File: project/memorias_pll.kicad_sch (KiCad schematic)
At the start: 34 parts, among them U5 M93C66, U6 ICE40HX4K-TQ144, U7 W25X40CLSN

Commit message: - Included properties such as Reference, Value, Footprint, and various manufacturer details. - Defined 20 pins with appropriate names and attributes for the symbol. - Ensured compatibility with KiCad version 8.0 and above.
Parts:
- D3: footprint Diode_SMD:D_1206_3216Metric -> (none)

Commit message: Agregados footprints de todos los componentes
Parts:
- D3: footprint (none) -> Diode_SMD:D_1206_3216Metric_Pad1.42x1.75mm_HandSolder
- D4: value LED -> LED Red; footprint libraries:WL-SMTW_3528 -> 150141RS73100(LED):LEDM3528X210N
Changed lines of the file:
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@@
 			)
 		)
-		(property "Value" "LED"
+		(property "Value" "LED Red"
 			(at 141.986 153.162 0)
 			(effects
@@
 			)
 		)
-		(property "Footprint" "libraries:WL-SMTW_3528"
+		(property "Footprint" "150141RS73100(LED):LEDM3528X210N"
 			(at 143.51 148.59 0)
 			(effects
@@
 			)
 		)
-		(property "Footprint" ""
+		(property "Footprint" "Diode_SMD:D_1206_3216Metric_Pad1.42x1.75mm_HandSolder"
 			(at 128.27 142.24 0)
 			(effects

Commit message: Ruteo critico finalizado
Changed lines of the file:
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@@
 (kicad_sch
-	(version 20231120)
+	(version 20250114)
 	(generator "eeschema")
-	(generator_version "8.0")
+	(generator_version "9.0")
 	(paper "A4")
+	(rectangle
+		(start 203.2 99.06)
+		(end 228.6 123.19)
+		(stroke
+			(width 0.25)
+			(type dash)
+		)
+		(fill
+			(type none)
+		)
+	)
+	(rectangle
+		(start 195.58 129.54)
+		(end 229.87 154.94)
+		(stroke
+			(width 0.25)
+			(type dash)
+		)
+		(fill
+			(type none)
+		)
+	)
+	(rectangle
+		(start 157.48 35.56)
+		(end 168.91 60.96)
+		(stroke
+			(width 0.25)
+			(type dash)
+		)
+		(fill
+			(type none)
+		)
+	)
+	(rectangle
+		(start 184.15 34.29)
+		(end 233.68 64.77)
+		(stroke
+			(width 0.25)
+			(type dash)
+		)
+		(fill
+			(type none)
+		)
+	)
+	(rectangle
+		(start 85.09 74.93)
+		(end 233.68 157.48)
+		(stroke
+			(width 0.25)
+			(type dash)
+		)
+		(fill
+			(type none)
+		)
+	)
+	(rectangle
+		(start 85.09 31.75)
+		(end 172.72 66.04)
+		(stroke
+			(width 0.25)
+			(type dash)
+		)
+		(fill
+			(type none)
+		)
+	)
+	(rectangle
+		(start 151.13 92.71)
+		(end 171.45 100.33)
+		(stroke
+			(width 0.25)
+			(type dash)
+		)
+		(fill
+			(type none)
+		)
+	)
+	(text "Desacople FPGA VCC\n"
+		(exclude_from_sim no)
+		(at 207.01 132.08 0)
+		(effects
+			(font
+				(size 1.27 1.27)
+			)
+		)
+	)
+	(text "R12 a R16 son de 220 Ohms"
+		(exclude_from_sim no)
+		(at 149.606 103.886 0)
+		(effects
+			(font
+				(size 1.27 1.27)
+			)
+			(justify left)
+		)
+	)
+	(text "Filtro PLL"
+		(exclude_from_sim no)
+		(at 189.738 36.83 0)
+		(effects
+			(font
+				(size 1.27 1.27)
+			)
+		)
+	)
+	(text "EEPROM"
+		(exclude_from_sim no)
+		(at 89.916 34.544 0)
+		(effects
+			(font
+				(size 1.27 1.27)
+			)
+		)
+	)
+	(text "R20 es un resistor de pull-up\nbasado en el esquemático de IceStick.\nRemover en caso de ser innecesario"
+		(exclude_from_sim no)
+		(at 179.832 87.63 0)
+		(effects
+			(font
+				(size 1.27 1.27)
+			)
+			(justify left)
+		)
+	)
+	(text "Desacople W25X40CLSN\n"
+		(exclude_from_sim no)
+		(at 215.646 101.854 0)
+		(effects
+			(font
+				(size 1.27 1.27)
+			)
+		)
+	)
+	(text "Memoria Flash y PLL"
+		(exclude_from_sim no)
+		(at 96.52 77.724 0)
+		(effects
+			(font
+				(size 1.27 1.27)
+			)
+		)
+	)
+	(text "Desacople M93C66"
+		(exclude_from_sim no)
+		(at 162.052 34.29 0)
+		(effects
+			(font
+				(size 1.27 1.27)
+			)
+		)
+	)
 	(junction
 		(at 217.17 52.07)
@@
 		)
 	)
-	(rectangle
-		(start 203.2 99.06)
-		(end 228.6 123.19)
-		(stroke
-			(width 0.25)
-			(type dash)
-		)
-		(fill
-			(type none)
-		)
-	)
-	(rectangle
-		(start 195.58 129.54)
-		(end 229.87 154.94)
-		(stroke
-			(width 0.25)
-			(type dash)
-		)
-		(fill
-			(type none)
-		)
-	)
-	(rectangle
-		(start 157.48 35.56)
-		(end 168.91 60.96)
-		(stroke
-			(width 0.25)
-			(type dash)
-		)
-		(fill
-			(type none)
-		)
-	)
-	(rectangle
-		(start 184.15 34.29)
-		(end 233.68 64.77)
-		(stroke
-			(width 0.25)
-			(type dash)
-		)
-		(fill
-			(type none)
-		)
-	)
-	(rectangle
-		(start 85.09 74.93)
-		(end 233.68 157.48)
-		(stroke
-			(width 0.25)
-			(type dash)
-		)
-		(fill
-			(type none)
-		)
-	)
-	(rectangle
-		(start 85.09 31.75)
-		(end 172.72 66.04)
-		(stroke
-			(width 0.25)
-			(type dash)
-		)
-		(fill
-			(type none)
-		)
-	)
-	(rectangle
-		(start 151.13 92.71)
-		(end 171.45 100.33)
-		(stroke
-			(width 0.25)
-			(type dash)
-		)
-		(fill
-			(type none)
-		)
-	)
-	(text "Desacople FPGA VCC\n"
-		(exclude_from_sim no)
-		(at 207.01 132.08 0)
-		(effects
-			(font
-				(size 1.27 1.27)
-			)
-		)
-	)
-	(text "R12 a R16 son de 220 Ohms"
-		(exclude_from_sim no)
-		(at 149.606 103.886 0)
-		(effects
-			(font
-				(size 1.27 1.27)
-			)
-			(justify left)
-		)
-	)
-	(text "Filtro PLL"
-		(exclude_from_sim no)
-		(at 189.738 36.83 0)
-		(effects
-			(font
-				(size 1.27 1.27)
-			)
-		)
-	)
-	(text "EEPROM"
-		(exclude_from_sim no)
-		(at 89.916 34.544 0)
-		(effects
-			(font
-				(size 1.27 1.27)
-			)
-		)
-	)
-	(text "R20 es un resistor de pull-up\nbasado en el esquemático de IceStick.\nRemover en caso de ser innecesario"
-		(exclude_from_sim no)
-		(at 179.832 87.63 0)
-		(effects
-			(font
-				(size 1.27 1.27)
-			)
-			(justify left)
-		)
-	)
-	(text "Desacople W25X40CLSN\n"
-		(exclude_from_sim no)
-		(at 215.646 101.854 0)
-		(effects
-			(font
-				(size 1.27 1.27)
-			)
-		)
-	)
-	(text "Memoria Flash y PLL"
-		(exclude_from_sim no)
-		(at 96.52 77.724 0)
-		(effects
-			(font
-				(size 1.27 1.27)
-			)
-		)
-	)
-	(text "Desacople M93C66"
-		(exclude_from_sim no)
-		(at 162.052 34.29 0)
-		(effects
-			(font
-				(size 1.27 1.27)
-			)
-		)
-	)
 	(label "VCCPLL1"
 		(at 222.25 48.26 0)
-		(fields_autoplaced yes)
 		(effects
 			(font
@@
 	(label "VCCPLL2"
 		(at 222.25 52.07 0)
-		(fields_autoplaced yes)
 		(effects
 			(font
@@
 	(label "GNDPLL2"
 		(at 223.52 62.23 0)
-		(fields_autoplaced yes)
 		(effects
 			(font
@@
 	(label "GNDPLL2"
 		(at 123.19 91.44 90)
-		(fields_autoplaced yes)
 		(effects
 			(font
@@
 	(label "VCCPLL2"
 		(at 123.19 133.35 270)
-		(fields_autoplaced yes)
 		(effects
 			(font
@@
 	(label "GNDPLL1"
 		(at 120.65 91.44 90)
-		(fields_autoplaced yes)
 		(effects
 			(font
@@
 	(label "GNDPLL1"
 		(at 222.25 38.1 0)
-		(fields_autoplaced yes)
 		(effects
 			(font
@@
 	(label "VCCPLL1"
 		(at 120.65 133.35 270)
-		(fields_autoplaced yes)
 		(effects
 			(font
@@
 		(shape input)
 		(at 153.67 90.17 90)
-		(fields_autoplaced yes)
 		(effects
 			(font
@@
 		(shape input)
 		(at 168.91 90.17 90)
-		(fields_autoplaced yes)
 		(effects
 			(font
@@
 		(shape input)
 		(at 107.95 45.72 180)
-		(fields_autoplaced yes)
 		(effects
 			(font
@@
 		(shape input)
 		(at 165.1 90.17 90)
-		(fields_autoplaced yes)
 		(effects
 			(font
@@
 		(shape output)
 		(at 100.33 111.76 180)
-		(fields_autoplaced yes)
 		(effects
 			(font
@@
 		(shape bidirectional)
 		(at 140.97 48.26 0)
-		(fields_autoplaced yes)
 		(effects
 			(font
@@
 		(shape output)
 		(at 161.29 90.17 90)
-		(fields_autoplaced yes)
 		(effects
 			(font
@@
 		(shape input)
 		(at 91.44 48.26 180)
-		(fields_autoplaced yes)
 		(effects
 			(font
@@
 		(shape input)
 		(at 115.57 57.15 180)
-		(fields_autoplaced yes)
 		(effects
 			(font
@@
 		(shape input)
 		(at 190.5 48.26 180)
-		(fields_autoplaced yes)
 		(effects
 			(font
@@
 		(shape input)
 		(at 130.81 45.72 0)
-		(fields_autoplaced yes)
 		(effects
 			(font
@@
 		(shape input)
 		(at 157.48 90.17 90)
-		(fields_autoplaced yes)
 		(effects
 			(font
@@
 		(dnp no)
 		(property "Reference" "R10"
-			(at 133.096 53.34 90)
+			(at 134.112 53.086 90)
 			(effects
 				(font
@@
 		)
 		(property "Value" "2k2"
-			(at 137.668 53.086 90)
+			(at 138.684 52.832 90)
 			(effects
 				(font
@@
 		)
 		(property "Value" "10k"
-			(at 137.668 58.42 90)
+			(at 133.604 60.706 90)
 			(effects
 				(font

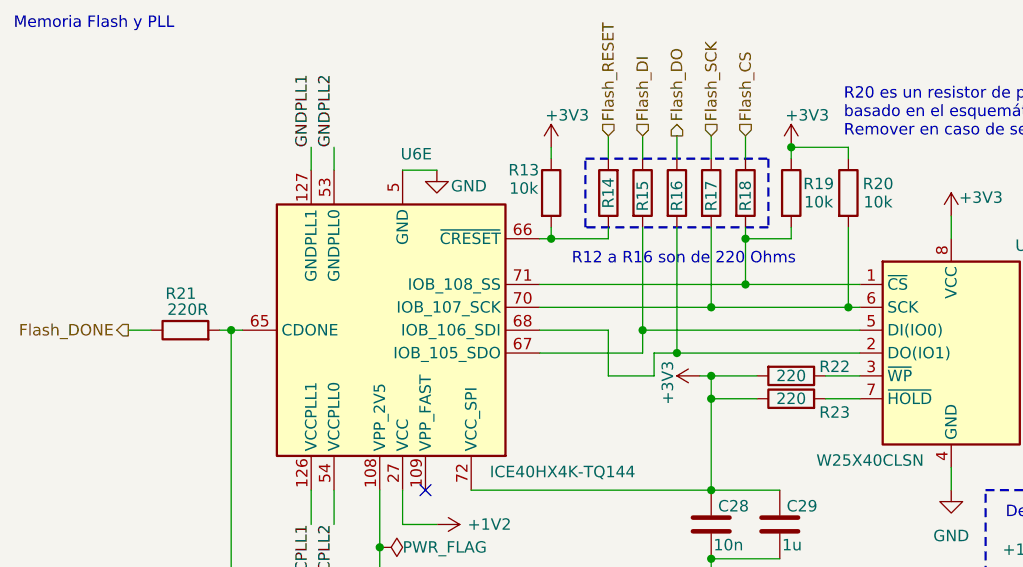
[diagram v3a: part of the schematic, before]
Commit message: Agregado de datasheets, cambio de regulador zener, ajuste de posicion de regulador, modelo 3d de oscilador
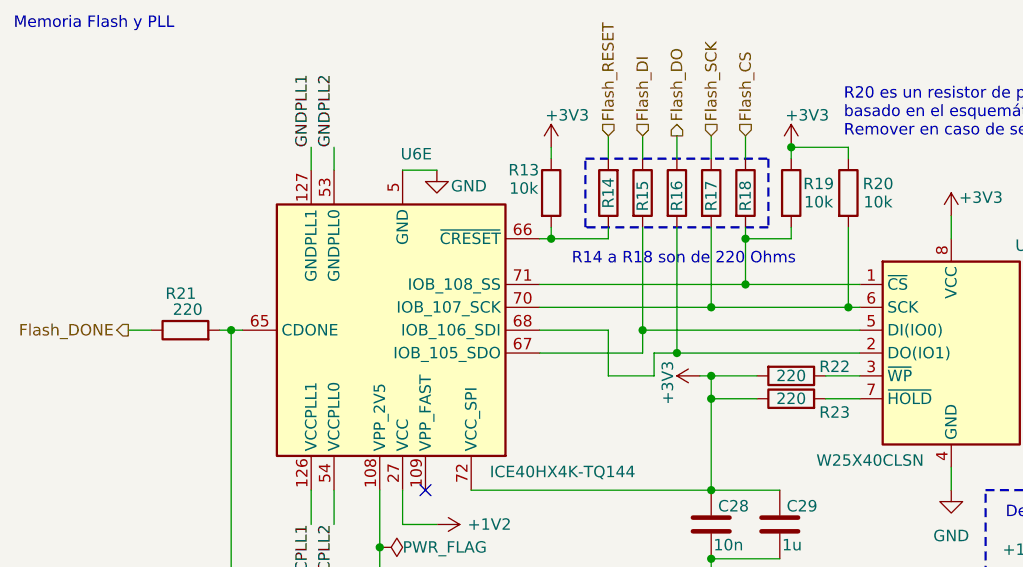
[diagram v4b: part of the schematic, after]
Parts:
- C21, C24: Código del fabricante (Order Code) (none) -> CL31B106KAHNNNE; Código del vendedor (Provider Order Code) (none) -> 187-CL31B106KAHNNNE; Fabricante (none) -> Samsung; Package (none) -> 1206
- C22, C23, C25, C30, C31, C32, C33: Código del fabricante (Order Code) (none) -> CL31B104KBCNFNC; Código del vendedor (Provider Order Code) (none) -> 187-CL31B104KBCNFNC; Fabricante (none) -> Samsung; Package (none) -> 1206
- C26, C28: Código del fabricante (Order Code) (none) -> CL31B103KHFNFNE; Código del vendedor (Provider Order Code) (none) -> 187-CL31B103KHFNFNE; Fabricante (none) -> Samsung; Package (none) -> 1206
- C27, C29: Código del fabricante (Order Code) (none) -> CL31B105KAHNFNE; Código del vendedor (Provider Order Code) (none) -> 187-CL31B105KAHNFNE; Fabricante (none) -> Samsung; Package (none) -> 1206
- D3: Código del fabricante (Order Code) (none) -> SD1206S040S1R0; Código del vendedor (Provider Order Code) (none) -> 581-SD1206S040S1R0; Fabricante (none) -> Kyocera AVX; Package (none) -> 1206
- D4: Código del fabricante (Order Code) (none) -> 150141RS73100; Código del vendedor (Provider Order Code) (none) -> 710-150141RS73100; Fabricante (none) -> Wurth Elektronik; Package (none) -> 3528
- R10: Código del fabricante (Order Code) (none) -> RC1206FR-072K2L; Código del vendedor (Provider Order Code) (none) -> 603-RC1206FR-072K2L; Fabricante (none) -> Yageo; Package (none) -> 1206
- R11, R9: Código del fabricante (Order Code) (none) -> AC1206FR-07100RL; Código del vendedor (Provider Order Code) (none) -> 603-AC1206FR-07100RL; Fabricante (none) -> Yageo; Package (none) -> 1206
- R12, R13, R19, R20: Código del fabricante (Order Code) (none) -> AC1206FR-0710KL; Código del vendedor (Provider Order Code) (none) -> 603-AC1206FR-0710KL; Fabricante (none) -> Yageo; Package (none) -> 1206
- R14, R22, R23: Código del fabricante (Order Code) (none) -> RC1206FR-13220RL; Código del vendedor (Provider Order Code) (none) -> 603-RC1206FR-13220RL; Fabricante (none) -> Yageo; Package (none) -> 1206
- R15, R16, R17, R18: value R -> 220; Código del fabricante (Order Code) (none) -> RC1206FR-13220RL; Código del vendedor (Provider Order Code) (none) -> 603-RC1206FR-13220RL; Fabricante (none) -> Yageo; Package (none) -> 1206
- R21: value 220R -> 220; Código del fabricante (Order Code) (none) -> RC1206FR-13220RL; Código del vendedor (Provider Order Code) (none) -> 603-RC1206FR-13220RL; Fabricante (none) -> Yageo; Package (none) -> 1206
- R24: Código del fabricante (Order Code) (none) -> RC1206FR-101KL; Código del vendedor (Provider Order Code) (none) -> 603-RC1206FR-101KL; Fabricante (none) -> Yageo; Package (none) -> 1206
- U5: Código del fabricante (Order Code) (none) -> M93C66-WMN6P; Código del vendedor (Provider Order Code) (none) -> 511-M93C66-WMN6P; Fabricante (none) -> ST; Package (none) -> SOIC-8
- U6: Código del fabricante (Order Code) (none) -> iCE40HX4K-TQ144; Código del vendedor (Provider Order Code) (none) -> 842-iCE40HX4K-TQ144; Fabricante (none) -> Lattice Semiconductor; Package (none) -> TQFP-144
- U7: Código del fabricante (Order Code) (none) -> W25X40CLSNIG; Código del vendedor (Provider Order Code) (none) -> 454-W25X40CLSNIG; Fabricante (none) -> Winbond; Package (none) -> SOIC-8
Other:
- note added: "R14 a R18 son de 220 Ohms"
- note removed: "R12 a R16 son de 220 Ohms"

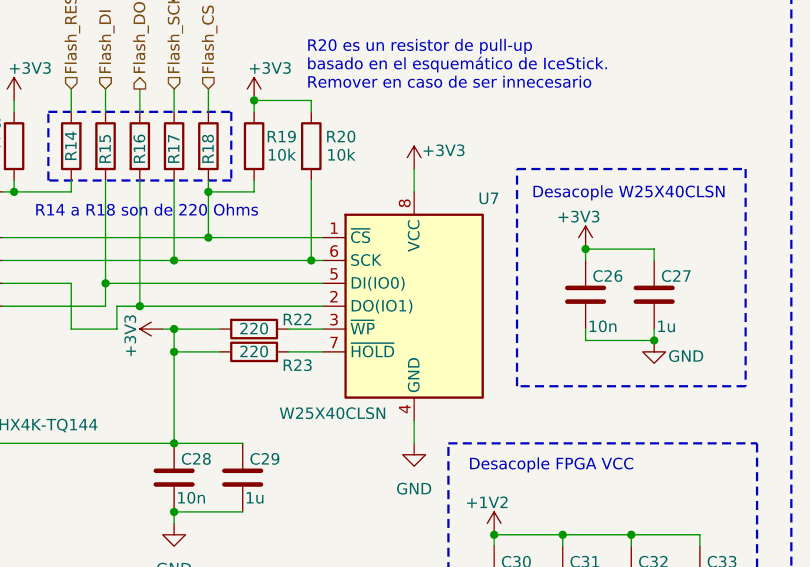
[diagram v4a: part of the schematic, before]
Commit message: Pistas, pads, soldermask y silkscreen corregidas para pasar analisis DMF de jlcpcb.
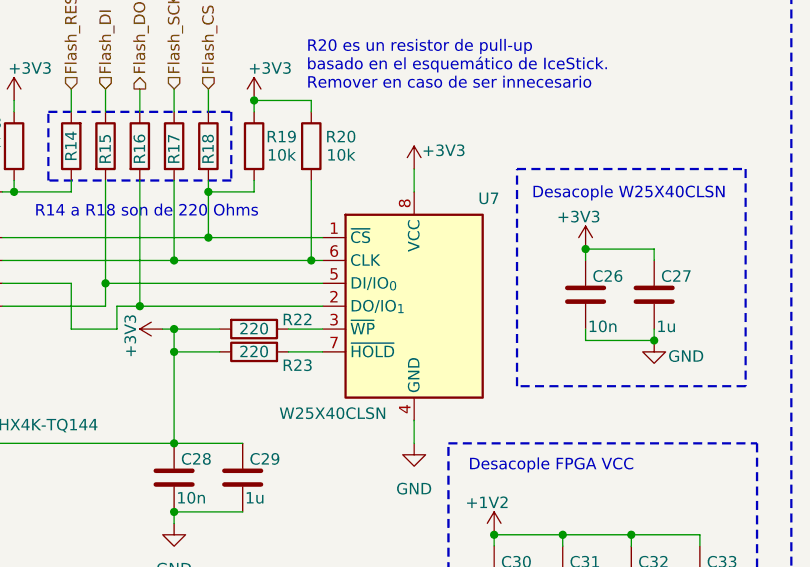
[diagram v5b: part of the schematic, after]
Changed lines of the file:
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@@
 			)
 		)
-		(property "Datasheet" "https://www.we-online.com/components/products/datasheet/150141RS73100.pdf"
+		(property "Datasheet" "~"
 			(at 143.51 148.59 0)
 			(effects
@@
 			)
 		)
+		(property "Sim.Pins" "1=K 2=A"
+			(at 143.51 148.59 0)
+			(effects
+				(font
+					(size 1.27 1.27)
+				)
+				(hide yes)
+			)
+		)
 		(pin "2"
 		)
@@
 			)
 		)
-		(property "Datasheet" "https://www.winbond.com/resource-files/w25x40cl_f%2020140325.pdf"
+		(property "Datasheet" "https://www.winbond.com/resource-files/W25X40CL_G%2020210505.pdf"
 			(at 194.31 88.9 0)
 			(effects
@@
 			)
 		)
-		(property "Description" "4Mbit Serial Flash memory, dual I/O SPI, SOIC-8"
+		(property "Description" "4Mbit / 512KiB Serial Flash memory, Standard/Dual I/O SPI, 2.3-3.6V, SOIC-8 (150 mil)"
 			(at 191.77 114.3 0)
 			(effects

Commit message: cambio a nombre final, agregado de licencia en esquematico y etiqueta
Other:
- company: (none) -> Maximiliano Simonazzi, Valentin Gomez Espeche
- title: (none) -> Azukar FPGA

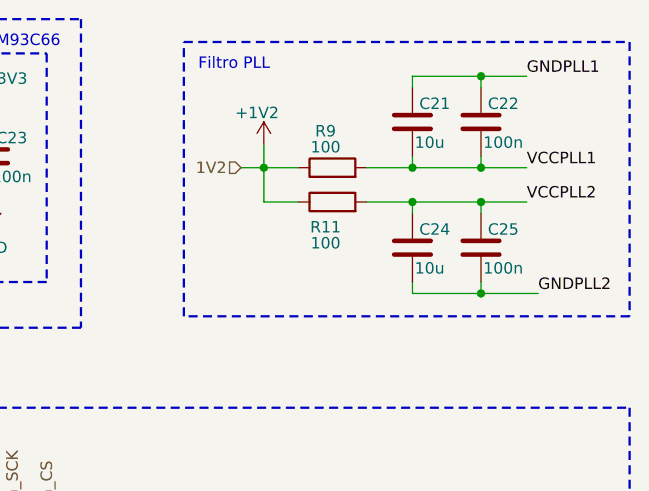
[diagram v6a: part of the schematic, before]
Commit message: Eliminar mensaje de error - Issue #8. Mejora en algunas trazas del PCB, eliminacion de algunas vias ordenando mejor los componentes.
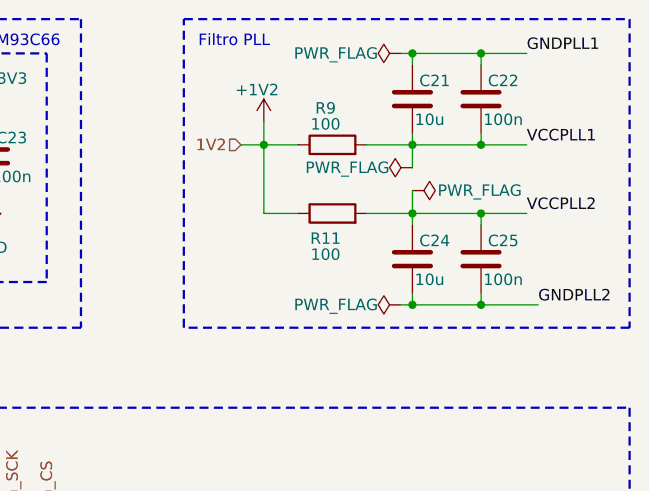
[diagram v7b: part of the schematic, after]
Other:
- moved on the sheet: C21, C22, C24, C25, R11, R9

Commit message: Version 2 de pcb completa, falta revisar silkscreen y ajustes menores
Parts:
- removed R14, R15, R16, R17, R18: 220, Resistor_SMD:R_1206_3216Metric, symbol Device:R
- renumbered C21 to C20, C22 to C21, C23 to C22, C24 to C23, C25 to C24, C26 to C25, C27 to C26, C28 to C27, C29 to C28, C30 to C29, C31 to C30, C32 to C31, C33 to C32, D3 to D2, D4 to D3, R9 to R14, R10 to R15, R11 to R16, R12 to R17, R13 to R18
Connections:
- net Flash_CS: now also R19.2, U6.71 (IOB_108_SS), U7.1 (~{CS})
- net Flash_DI: now also U6.67 (IOB_105_SDO), U7.5 (DI/IO_{0})
- net Flash_DO: now also U6.68 (IOB_106_SDI), U7.2 (DO/IO_{1})
- net Flash_RESET: now also R18.2, U6.66 (~{CRESET})
- net Flash_SCK: now also R20.2, U6.70 (IOB_107_SCK), U7.6 (CLK)
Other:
- note added: "R20 No es necesario. El esquemático de IceStick lo contiene por eso lo consideramos."
- note removed: "R14 a R18 son de 220 Ohms"
- note removed: "R20 es un resistor de pull-up basado en el esquemático de IceStick. Remover en caso de ser innecesario"
- moved on the sheet: C25, C26, R19, R20, U7
